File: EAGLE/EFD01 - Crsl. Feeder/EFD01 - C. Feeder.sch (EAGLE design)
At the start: 34 parts, among them J1 MOD TOOL, J2 SPI, J3 MOT, J4 FTDI, Q1 BSS138, Q2 16MHz, U1 SP3485, U2 TCST1030, U3 ATMEGA238, U4 DRV8825

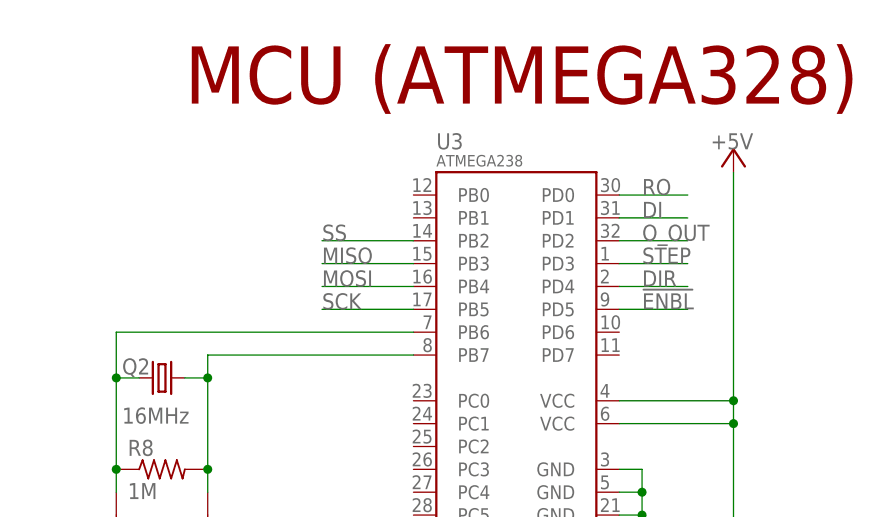
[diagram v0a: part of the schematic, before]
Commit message: Created preliminary final schematic for ECA03
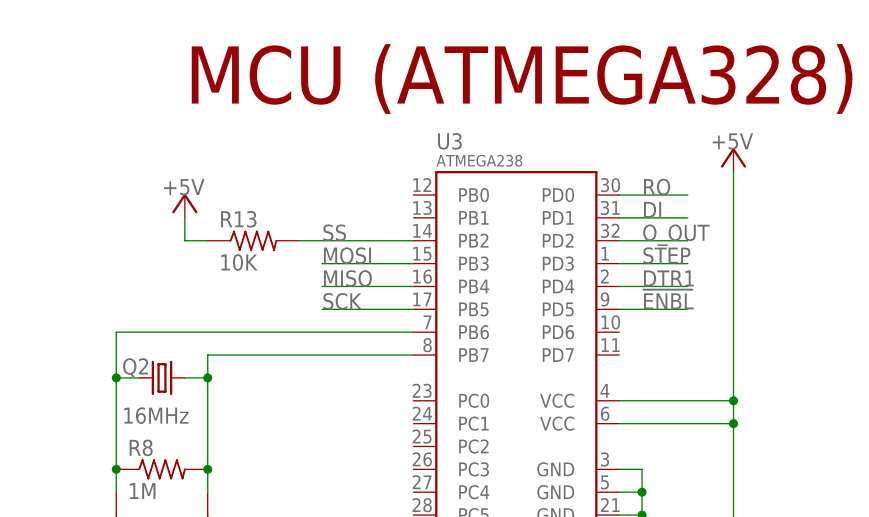
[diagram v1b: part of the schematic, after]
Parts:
- added R13: 10K, TinWhiskers:CPL-RES-0603-10K-0.1W
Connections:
- net +5V: now also R13.1
- net DIR: no longer U3.PD4
- net DTR1: now also U3.PD4
- net MISO: now also U3.PB4; no longer U3.PB3
- net MOSI: now also U3.PB3; no longer U3.PB4
- net SS: now also R13.2
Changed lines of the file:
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@@
 <part name="LOGO2" library="FirePick" deviceset="LOGO-FIREPICK" device="LARGE"/>
 <part name="SUPPLY17" library="TinWhiskers" deviceset="GND" device=""/>
+<part name="R13" library="TinWhiskers" deviceset="CPL-RES-0603-10K-0.1W" device="" value="10K"/>
+<part name="P+13" library="supply1" deviceset="+5V" device=""/>
 </parts>
 <sheets>
@@
 <instance part="LOGO2" gate="G$1" x="81.28" y="10.16"/>
 <instance part="SUPPLY17" gate="GND" x="350.52" y="45.72"/>
+<instance part="R13" gate="G$1" x="294.64" y="193.04"/>
+<instance part="P+13" gate="1" x="287.02" y="198.12" smashed="yes">
+<attribute name="VALUE" x="284.48" y="198.12" size="1.778" layer="96"/>
+</instance>
 </instances>
 <busses>
@@
 <pinref part="P+12" gate="1" pin="+5V"/>
 </segment>
+<segment>
+<pinref part="P+13" gate="1" pin="+5V"/>
+<wire x1="287.02" y1="195.58" x2="287.02" y2="193.04" width="0.1524" layer="91"/>
+<pinref part="R13" gate="G$1" pin="1"/>
+<wire x1="287.02" y1="193.04" x2="289.56" y2="193.04" width="0.1524" layer="91"/>
+</segment>
 </net>
 <net name="!ENBL" class="0">
@@
 <label x="73.66" y="81.28" size="1.778" layer="95" ratio="12"/>
 </segment>
+<segment>
+<pinref part="U3" gate="G$1" pin="PD4"/>
+<wire x1="335.28" y1="187.96" x2="342.9" y2="187.96" width="0.1524" layer="91"/>
+<label x="337.82" y="187.96" size="1.778" layer="95" ratio="12"/>
+</segment>
 </net>
 <net name="STEP" class="0">
@@
 <label x="342.9" y="73.66" size="1.778" layer="95" ratio="12"/>
 </segment>
-<segment>
-<pinref part="U3" gate="G$1" pin="PD4"/>
-<wire x1="335.28" y1="187.96" x2="342.9" y2="187.96" width="0.1524" layer="91"/>
-<label x="337.82" y="187.96" size="1.778" layer="95" ratio="12"/>
-</segment>
 </net>
 <net name="MISO" class="0">
@@
 </segment>
 <segment>
+<pinref part="U3" gate="G$1" pin="PB4"/>
+<wire x1="312.42" y1="187.96" x2="302.26" y2="187.96" width="0.1524" layer="91"/>
+<label x="302.26" y="187.96" size="1.778" layer="95" ratio="12"/>
+</segment>
+</net>
+<net name="SCK" class="0">
+<segment>
+<pinref part="J2" gate="G$1" pin="3"/>
+<wire x1="124.46" y1="152.4" x2="129.54" y2="152.4" width="0.1524" layer="91"/>
+<label x="124.46" y="152.4" size="1.778" layer="95" ratio="12"/>
+</segment>
+<segment>
+<pinref part="U3" gate="G$1" pin="PB5"/>
+<wire x1="312.42" y1="185.42" x2="302.26" y2="185.42" width="0.1524" layer="91"/>
+<label x="302.26" y="185.42" size="1.778" layer="95" ratio="12"/>
+</segment>
+</net>
+<net name="MOSI" class="0">
+<segment>
+<pinref part="J2" gate="G$1" pin="4"/>
+<wire x1="124.46" y1="149.86" x2="129.54" y2="149.86" width="0.1524" layer="91"/>
+<label x="124.46" y="149.86" size="1.778" layer="95" ratio="12"/>
+</segment>
+<segment>
 <pinref part="U3" gate="G$1" pin="PB3"/>
 <wire x1="312.42" y1="190.5" x2="302.26" y2="190.5" width="0.1524" layer="91"/>
 <label x="302.26" y="190.5" size="1.778" layer="95" ratio="12"/>
-</segment>
-</net>
-<net name="SCK" class="0">
-<segment>
-<pinref part="J2" gate="G$1" pin="3"/>
-<wire x1="124.46" y1="152.4" x2="129.54" y2="152.4" width="0.1524" layer="91"/>
-<label x="124.46" y="152.4" size="1.778" layer="95" ratio="12"/>
-</segment>
-<segment>
-<pinref part="U3" gate="G$1" pin="PB5"/>
-<wire x1="312.42" y1="185.42" x2="302.26" y2="185.42" width="0.1524" layer="91"/>
-<label x="302.26" y="185.42" size="1.778" layer="95" ratio="12"/>
-</segment>
-</net>
-<net name="MOSI" class="0">
-<segment>
-<pinref part="J2" gate="G$1" pin="4"/>
-<wire x1="124.46" y1="149.86" x2="129.54" y2="149.86" width="0.1524" layer="91"/>
-<label x="124.46" y="149.86" size="1.778" layer="95" ratio="12"/>
-</segment>
-<segment>
-<pinref part="U3" gate="G$1" pin="PB4"/>
-<wire x1="312.42" y1="187.96" x2="302.26" y2="187.96" width="0.1524" layer="91"/>
-<label x="302.26" y="187.96" size="1.778" layer="95" ratio="12"/>
 </segment>
 </net>
@@
 <segment>
 <pinref part="U3" gate="G$1" pin="PB2"/>
-<wire x1="312.42" y1="193.04" x2="302.26" y2="193.04" width="0.1524" layer="91"/>
+<wire x1="312.42" y1="193.04" x2="299.72" y2="193.04" width="0.1524" layer="91"/>
 <label x="302.26" y="193.04" size="1.778" layer="95" ratio="12"/>
-</segment>
-</net>
+<pinref part="R13" gate="G$1" pin="2"/>
+</segment>
+</net>

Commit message: Preliminary placement and routing done for EFD01. Preliminary placement done for EMC03. All schematics are ready for review (A0 for ECAM03 needs to be defined, also SS for EFD01, ECAM03, etc.)
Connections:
- removed net !ENBL: U3.PD5, U4.!ENBL
- net !ENABLE: now also U3.PD5, U4.!ENBL
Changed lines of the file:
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@@
-</segment>
-</net>
-<net name="!ENBL" class="0">
-<segment>
-<pinref part="U4" gate="G$1" pin="!ENBL"/>
-<wire x1="340.36" y1="68.58" x2="347.98" y2="68.58" width="0.1524" layer="91"/>
-<label x="342.9" y="68.58" size="1.778" layer="95" ratio="12"/>
-</segment>
-<segment>
-<pinref part="U3" gate="G$1" pin="PD5"/>
-<wire x1="335.28" y1="185.42" x2="342.9" y2="185.42" width="0.1524" layer="91"/>
-<label x="337.82" y="185.42" size="1.778" layer="95" ratio="12"/>
 </segment>
 </net>
@@
 <label x="125.984" y="86.36" size="1.778" layer="95" ratio="12"/>
 </segment>
-</net>
+<segment>
+<pinref part="U3" gate="G$1" pin="PD5"/>
+<wire x1="335.28" y1="185.42" x2="342.9" y2="185.42" width="0.1524" layer="91"/>
+<label x="337.82" y="185.42" size="1.778" layer="95" ratio="12"/>
+</segment>
+<segment>
+<pinref part="U4" gate="G$1" pin="!ENBL"/>
+<wire x1="340.36" y1="68.58" x2="347.98" y2="68.58" width="0.1524" layer="91"/>
+<label x="342.9" y="68.58" size="1.778" layer="95" ratio="12"/>
+</segment>
+</net>

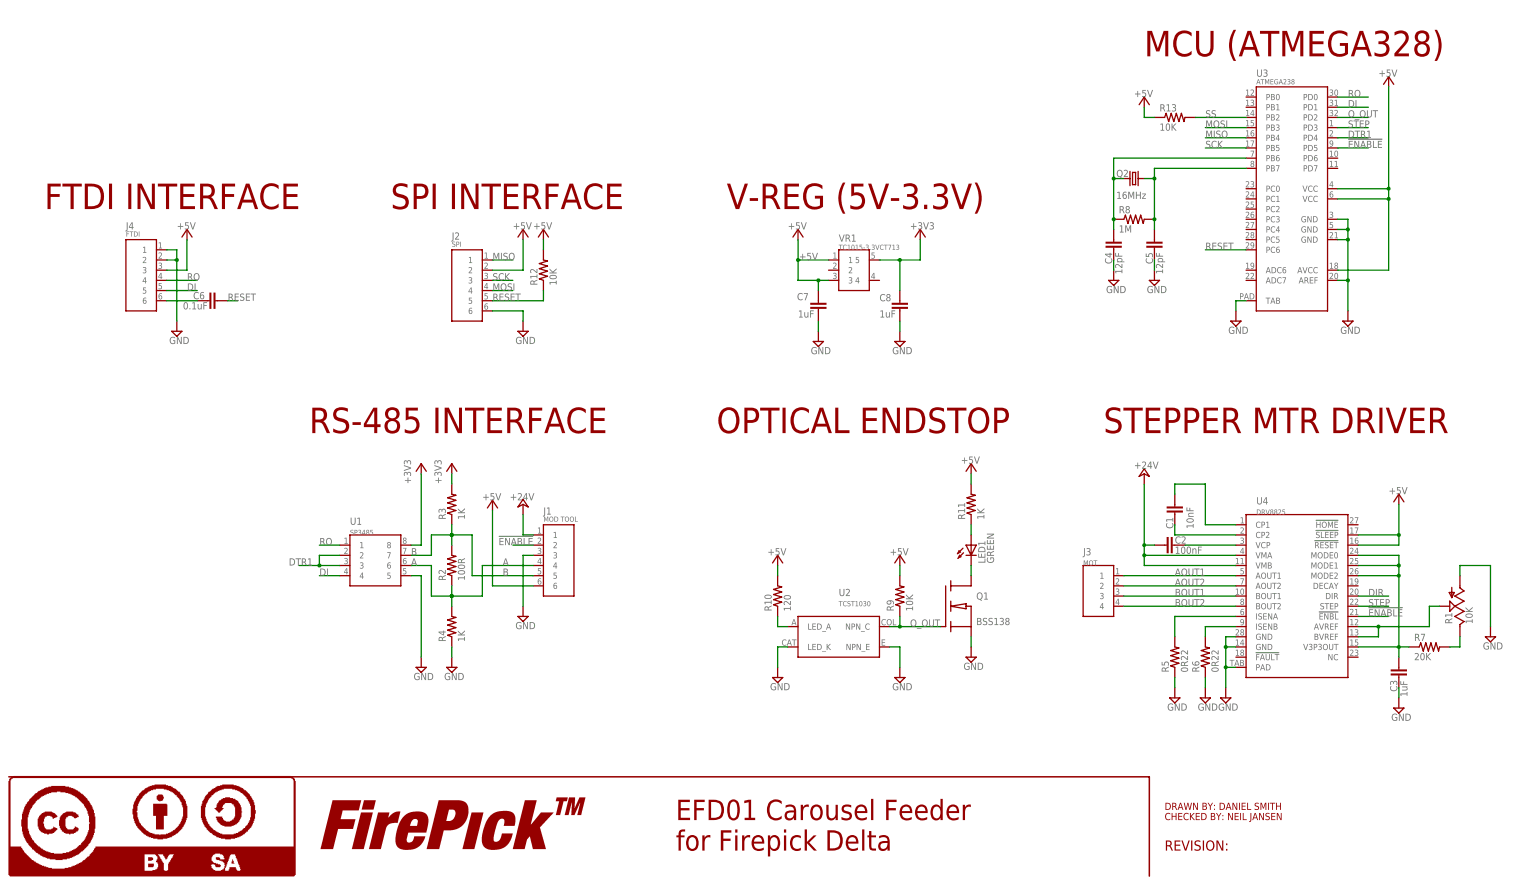
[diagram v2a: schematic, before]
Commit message: Finalized schematics (minus potential LDO regulator) for all boards. Layout partially done for EFD01
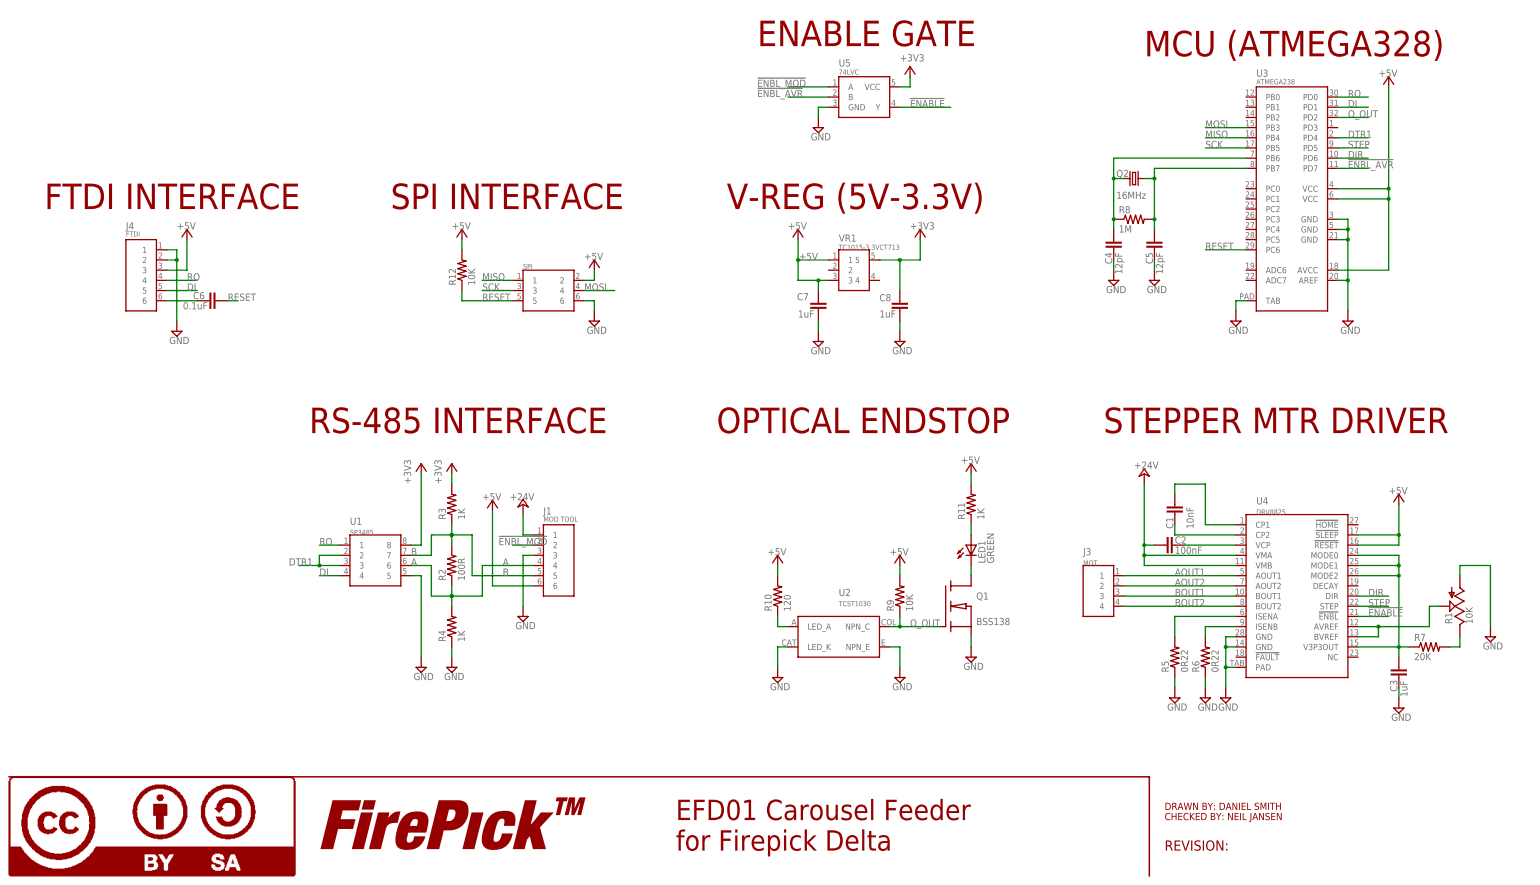
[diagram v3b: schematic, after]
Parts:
- removed R13: 10K, TinWhiskers:CPL-RES-0603-10K-0.1W
- added U5: 74LVC, TinWhiskers:CPL-IC-LOGIC-OR-1CH-74LVC
- J2: device TinWhiskers:CPL-CON-HEADER-0.1IN-6P-M -> TinWhiskers:CPL-CON-HEADER-0.1IN-2X3P-M; PARTNO 67996-206HLF -> (none)
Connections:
- removed net SS: R13.2, U3.PB2
- new net !ENBL_AVR: U3.PD7, U5.B
- new net !ENBL_MOD: J1.2, U5.A
- net !ENABLE: now also U5.Y; no longer J1.2, U3.PD5
- net +3V3: now also U5.VCC
- net +5V: no longer R13.1
- net DIR: now also U3.PD6
- net GND: now also U5.GND
- net STEP: now also U3.PD5; no longer U3.PD3
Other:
- note added: "ENABLE GATE"
- note added: "SPI"
- moved on the sheet: R12

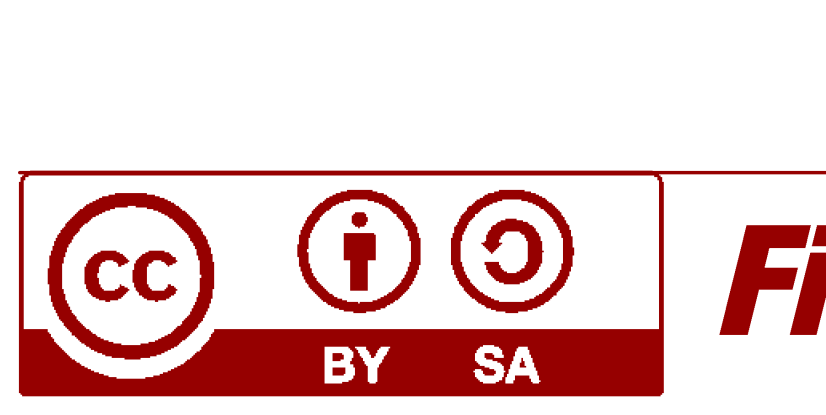
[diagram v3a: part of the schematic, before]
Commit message: Routed EFD01, ECAM03 boards. Modification needs to be made for hole/keepout in ECAM03. EMC03 X and Y sides routed. Will need to increase some trace widths.
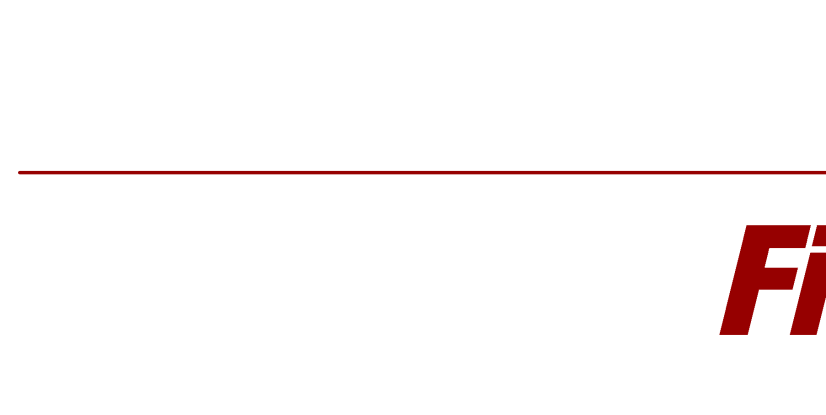
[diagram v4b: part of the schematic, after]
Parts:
- removed LOGO1: LOGO-CC-BY-SALARGE, FirePick:LOGO-CC-BY-SALARGE
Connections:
- net N$7 renamed VCP
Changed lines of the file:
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@@
 <attribute name="PARTNO" value="UMK107B7104KA-T"/>
 </part>
-<part name="LOGO1" library="FirePick" deviceset="LOGO-CC-BY-SA" device="LARGE"/>
 <part name="LOGO2" library="FirePick" deviceset="LOGO-FIREPICK" device="LARGE"/>
 <part name="SUPPLY17" library="TinWhiskers" deviceset="GND" device=""/>
@@
 <attribute name="PARTNO" x="55.88" y="147.32" size="2.54" layer="96" ratio="10" display="off"/>
 </instance>
-<instance part="LOGO1" gate="G$1" x="3.81" y="3.81"/>
 <instance part="LOGO2" gate="G$1" x="81.28" y="10.16"/>
 <instance part="SUPPLY17" gate="GND" x="350.52" y="45.72"/>
@@
 </segment>
 </net>
-<net name="N$7" class="0">
+<net name="VCP" class="0">
 <segment>
 <pinref part="U4" gate="G$1" pin="VCP"/>

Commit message: Updated all boards to include changes for production
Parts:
- J4: device TinWhiskers:CPL-CON-JST-2.0MM-6P-M-RA -> TinWhiskers:CPL-CON-HEADER-0.1IN-6P-M
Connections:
- net GND: no longer U3.TAB
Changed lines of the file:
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@@
 <part name="SUPPLY10" library="TinWhiskers" deviceset="GND" device=""/>
 <part name="P+7" library="supply1" deviceset="+5V" device=""/>
-<part name="SUPPLY11" library="TinWhiskers" deviceset="GND" device=""/>
 <part name="SUPPLY12" library="TinWhiskers" deviceset="GND" device=""/>
 <part name="P+8" library="supply1" deviceset="+5V" device=""/>
@@
 <attribute name="PARTNO" value="RC0603FR-0710KL"/>
 </part>
-<part name="J4" library="TinWhiskers" deviceset="CPL-CON-JST-2.0MM-6P-M-RA" device="" value="FTDI">
+<part name="J4" library="TinWhiskers" deviceset="CPL-CON-HEADER-0.1IN-6P-M" device="" value="FTDI">
 <attribute name="PARTNO" value="S6B-PH-SM4-TB(LF)(SN)"/>
 </part>
@@
 <attribute name="VALUE" x="345.44" y="203.2" size="1.778" layer="96"/>
 </instance>
-<instance part="SUPPLY11" gate="GND" x="309.88" y="142.24"/>
 <instance part="SUPPLY12" gate="GND" x="337.82" y="142.24"/>
 <instance part="P+8" gate="1" x="195.58" y="83.82" smashed="yes">
@@
 </segment>
 <segment>
-<pinref part="U3" gate="G$1" pin="TAB"/>
-<wire x1="312.42" y1="147.32" x2="309.88" y2="147.32" width="0.1524" layer="91"/>
-<wire x1="309.88" y1="147.32" x2="309.88" y2="144.78" width="0.1524" layer="91"/>
-<pinref part="SUPPLY11" gate="GND" pin="GND"/>
-</segment>
-<segment>

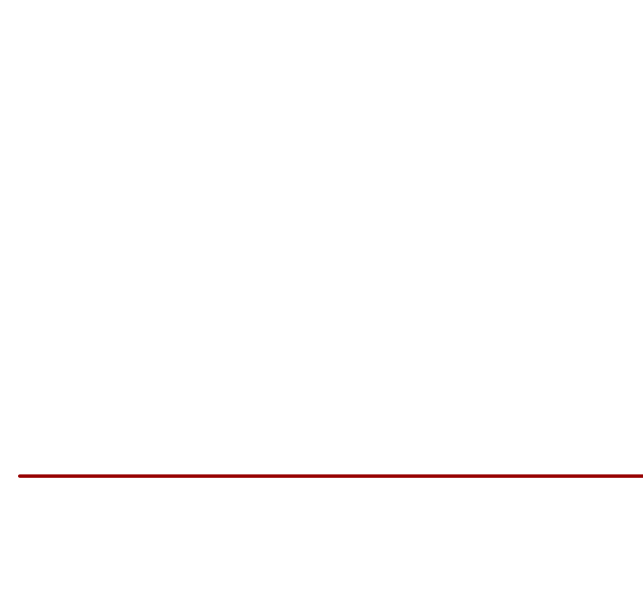
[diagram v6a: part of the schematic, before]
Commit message: Made some simple adjustments (moved traces, increased width on current carrying components).  Added P/N and TW logo.  Generated gerbers for Rev--.
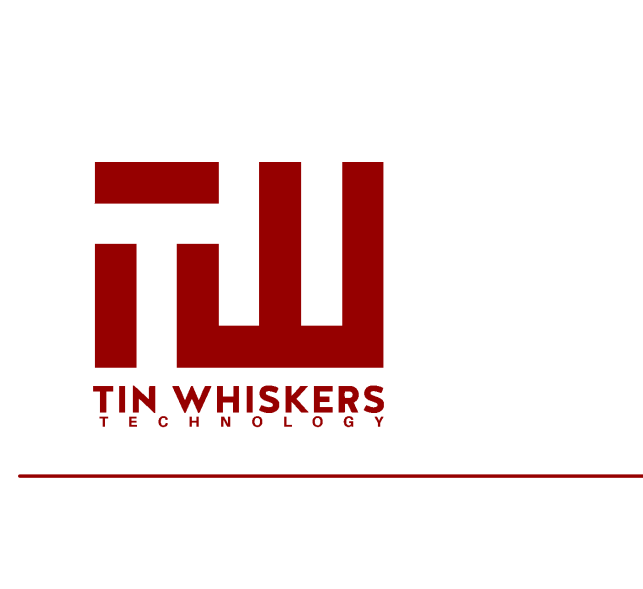
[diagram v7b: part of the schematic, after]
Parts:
- added U$1: TIN-WHISKERSSMALL, !tin-whiskers-logo:TIN-WHISKERSSMALL
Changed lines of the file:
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@@
 <?xml version="1.0" encoding="utf-8"?>
 <!DOCTYPE eagle SYSTEM "eagle.dtd">
-<eagle version="7.4.0">
+<eagle version="7.3.0">
 <drawing>
 <settings>
@@
 <part name="P+11" library="supply1" deviceset="+5V" device=""/>
 <part name="SUPPLY4" library="TinWhiskers" deviceset="GND" device=""/>
+<part name="U$1" library="!tin-whiskers-logo" deviceset="TIN-WHISKERS" device="SMALL"/>
 </parts>
 <sheets>
@@
 <attribute name="VALUE" x="147.955" y="139.065" size="1.778" layer="96"/>
 </instance>
+<instance part="U$1" gate="G$1" x="10.16" y="33.02"/>
 </instances>
 <busses>
